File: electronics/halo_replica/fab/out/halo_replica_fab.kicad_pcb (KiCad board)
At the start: 4 copper layers, 30 x 30 mm, 45 parts, among them J1 VOICE COIL / SOUNDER, J2 NFC COIL 13.56MHz, J3 SWD (nRST SWDIO SWCLK GND VBA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, U1 nRF52832-QFAA-R, U2 MIC94090YC6 (0.5 uA, 1.5 A), U3 MX25R3235F 32Mb 1.65-3.6V, U4 SC7A20 3-axis, LGA-12, U5 MAX98357A class-D, TQFN-16, X1 32MHz 10ppm CL=8pF, X2 32.768kHz 20ppm CL=12.5pF

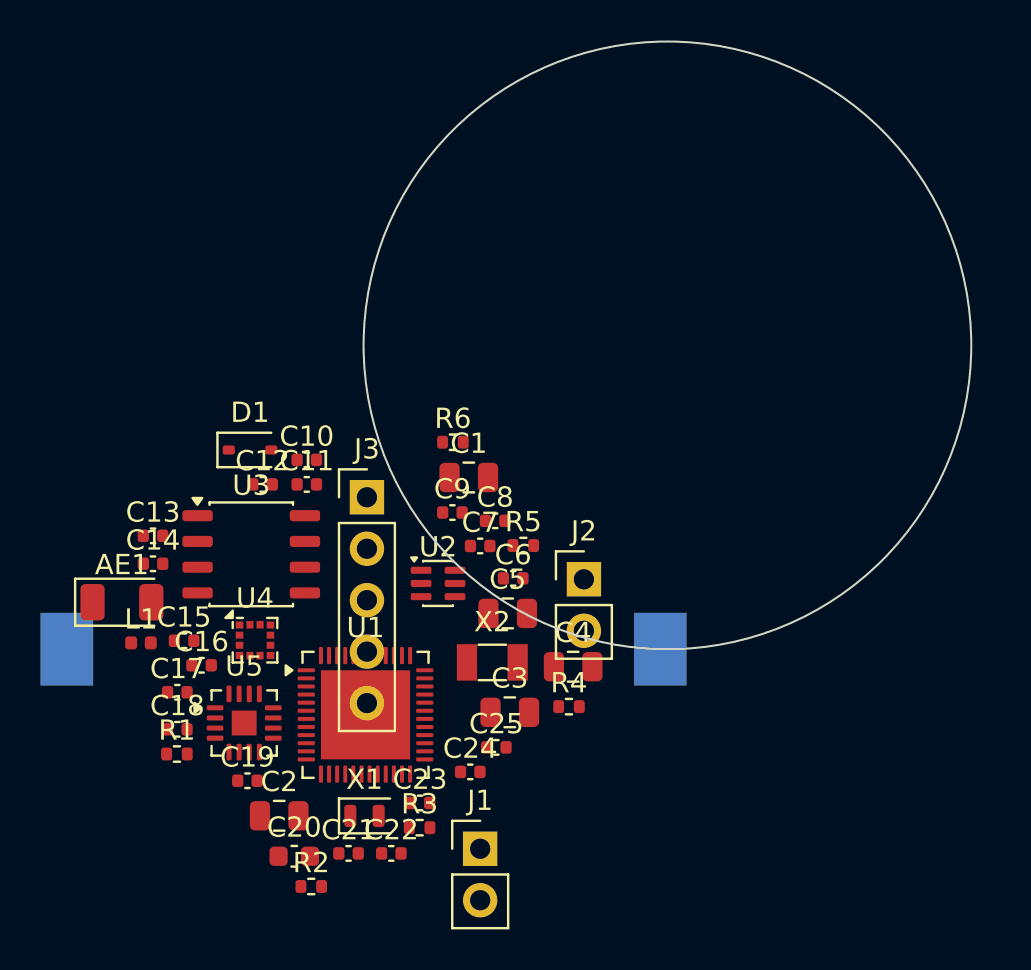
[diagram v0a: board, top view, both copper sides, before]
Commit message: L11: the resolver was leaving its scratch file in the repository
`_bom-tmp.csv` was committed in ab9315d. x_lcsc_resolve needs an intermediate
BOM and it wrote it BESIDE the real deliverable — so a throwaway landed in
out/schematic-fab/ next to the files someone is meant to send to a fab, named
"tmp" and tracked by git.

Fixed at the cause rather than by deleting it: the intermediate goes to a
tempfile.mkdtemp and is removed in a finally. Untracked and removed from disk.

Small, but the failure mode is not: a fab bundle is a folder somebody zips and
emails, and the whole discipline of cepcb.fab is that what is in that folder is
what was checked. A file whose name says "ignore me" undermines that more than
its size suggests.

AND A PROCESS NOTE I HAVE NOW EARNED TWICE. Both this fix and the previous
correction were nearly lost to the same shell mistake: a compound command
starting with a RELATIVE `cd` into a directory the session was already in.
`cd X; rest` runs the rest from the wrong place and reports success. Once it
silently skipped a file edit whose completion I then claimed in a commit
message (corrected in 0a91f02); once it silently skipped the `git add` while a
later `git push` printed "pushed" for ANOTHER LANE'S COMMIT, which is the more
dangerous of the two because the output looked like success for my work.
Absolute paths from here.

Self-test PASS. The fidelity sheet's checks still 7/7, 13 MEASURED.

Co-Authored-By: Claude Opus 5 (1M context) <noreply@anthropic.com>
Claude-Session: https://claude.ai/code/session_013mLHcufSVJ7BYZ5QCYysr1
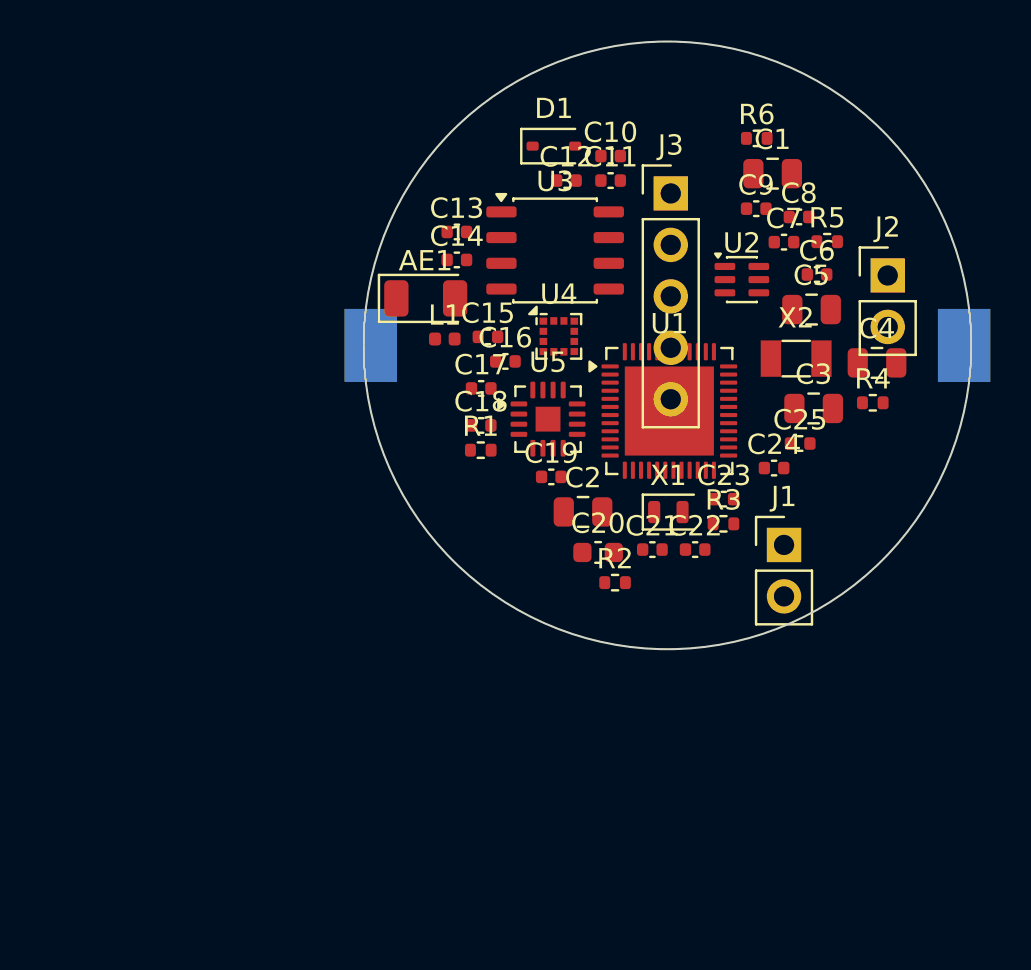
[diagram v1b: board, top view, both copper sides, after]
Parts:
- moved C23 21.2 mm to (17.8, 22.6)
- moved X1 21.2 mm to (15.0, 23.2)
- moved BT1 21.2 mm to (15.0, 15.0)
- moved C1 21.2 mm to (20.2, 6.52)
- moved C4 21.2 mm to (25.3, 15.9)
- moved C5 21.2 mm to (22.1, 13.2)
- moved C6 21.2 mm to (22.4, 11.5)
- moved C8 21.2 mm to (21.5, 8.66)
- moved C9 21.2 mm to (19.4, 8.25)
- moved J1 21.2 mm to (20.8, 24.9)
- moved J2 21.2 mm to (25.9, 11.5)
- moved J3 21.2 mm to (15.2, 7.50)
- moved R3 21.2 mm to (17.8, 23.8)
- moved R4 21.2 mm to (25.1, 17.8)
- moved R5 21.2 mm to (22.9, 9.88)
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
